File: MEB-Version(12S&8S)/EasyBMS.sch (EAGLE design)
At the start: 146 parts, among them IC1 XL7046, IC2 LTC6811IG-1#PBF, IC3 ESP32-S3-WROOM-1-N4R2, IC4 C98655, J1 TYPE-C-31-M-12, Q14 C8547, Q15 C8547, Q16 C8547, Q18 C8547, Q20 C8547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

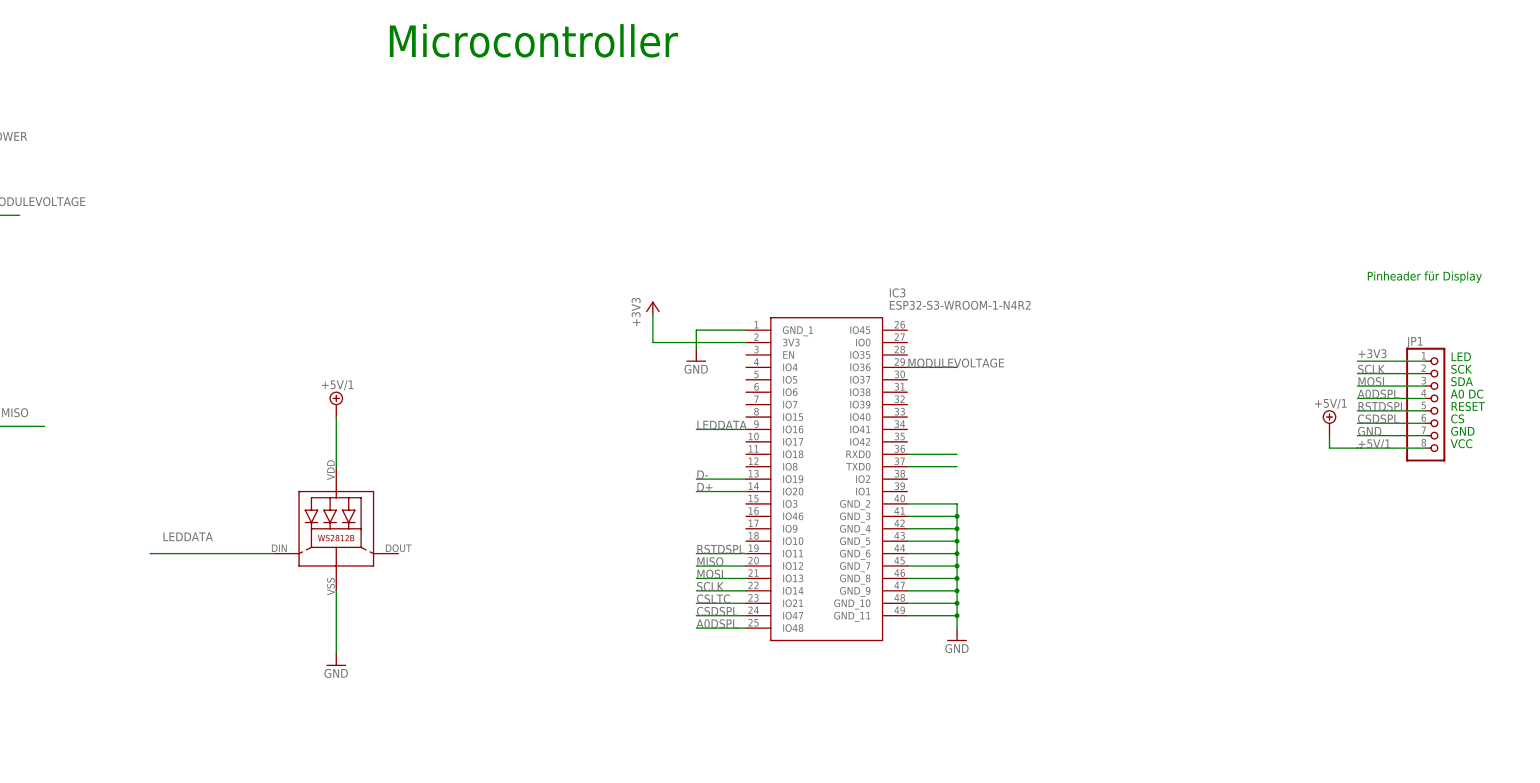
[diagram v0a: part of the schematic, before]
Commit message: add libraries folder with ESP32-C6 lib and change ESP32-S3 to ESP32-C6 MCU
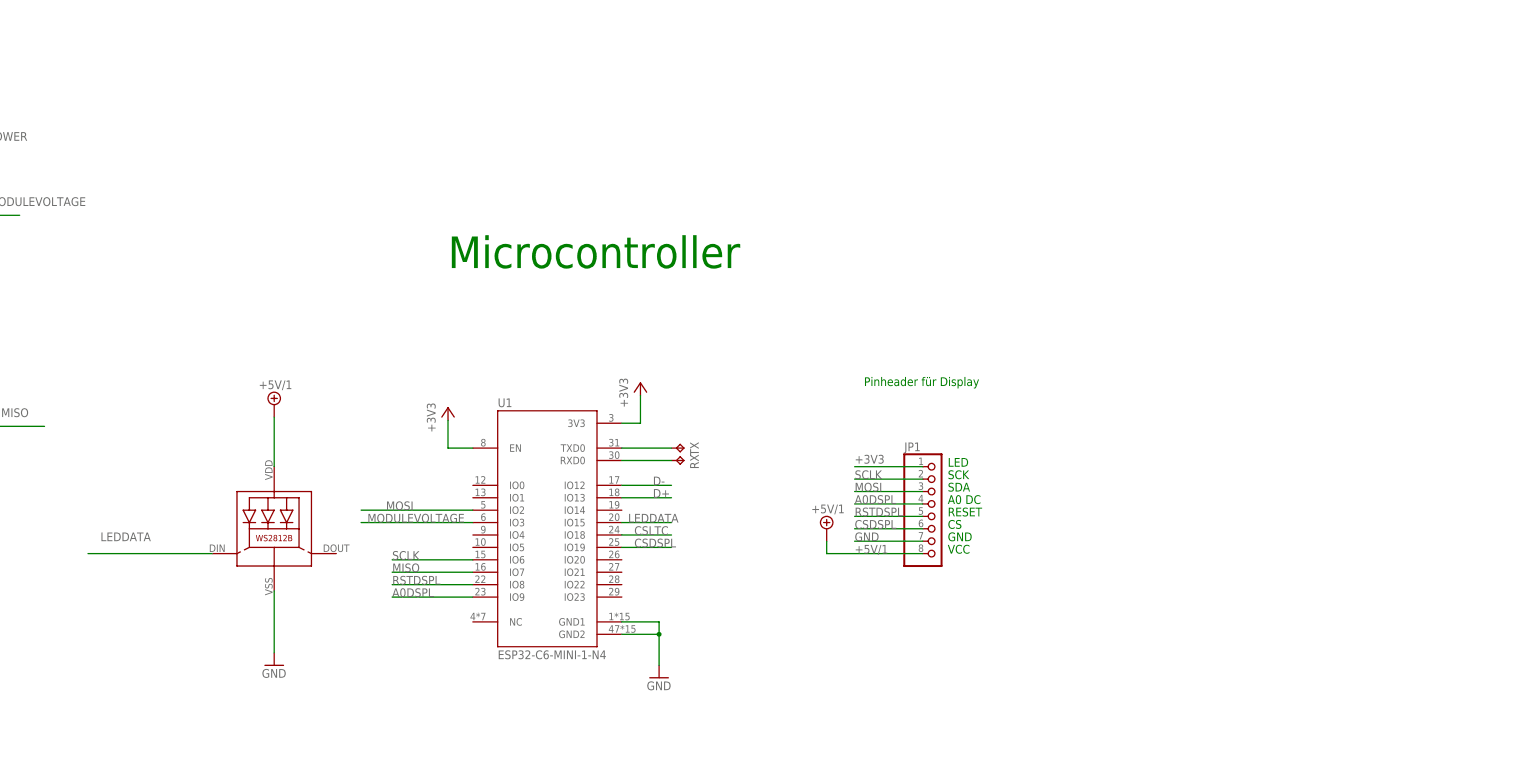
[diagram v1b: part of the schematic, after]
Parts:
- removed IC3: ESP32-S3-WROOM-1-N4R2, SamacSys_Parts:ESP32-S3-WROOM-1-N4R2
- added RX, TX: TPB2,54, testpad:TPB2,54
- added U1: ESP32-C6-MINI-1-N4, ESP32-C6-MINI-1-N4:ESP32-C6-MINI-1-N4
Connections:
- removed net N$51: IC3.RXD0
- removed net N$52: IC3.TXD0
- new net N$10: RX.TP, U1.RXD0
- new net N$2: TX.TP, U1.TXD0
- net +3V3: now also U1.3V3, U1.EN; no longer IC3.3V3
- net A0DSPL: now also U1.IO9; no longer IC3.IO48
- net CSDSPL: now also U1.IO19; no longer IC3.IO47
- net CSLTC: now also U1.IO18; no longer IC3.IO21
- net D+: now also U1.IO13; no longer IC3.IO20
- net D-: now also U1.IO12; no longer IC3.IO19
- net GND: now also U1.GND1, U1.GND2; no longer IC3.GND_1, IC3.GND_10, IC3.GND_11, IC3.GND_2, IC3.GND_3, IC3.GND_4, IC3.GND_5, IC3.GND_6, IC3.GND_7, IC3.GND_8, IC3.GND_9
- net LEDDATA: now also U1.IO15; no longer IC3.IO16
- net MISO: now also U1.IO7; no longer IC3.IO12
- net MODULEVOLTAGE: now also U1.IO3; no longer IC3.IO36
- net MOSI: now also U1.IO2; no longer IC3.IO13
- net RSTDSPL: now also U1.IO8; no longer IC3.IO11
- net SCLK: now also U1.IO6; no longer IC3.IO14
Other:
- moved on the sheet: JP1

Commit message: new version v3.0 review layout, change some parts and add isolated CAN-transceiver
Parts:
- added C10, C11: 100nF, rcl:C-EUC0402
- added C12: 47µF, rcl:C-EUC1206
- added C9: (no value), rcl:CPOL-EU153CLV-0605
- added CS1, CSLTC, MISO: (no value), jumper:SJ
- added IC3: ISO1042DWV, ISO1042DWV:ISO1042DWV
- added JP7: 2828XX-4282834-4, Connector:2828XX-4282834-4
- added R12: 120R, rcl:R-EU_R0402
- C1, C19, C4, C5, C7, C8: device rcl:C-EUC1206 -> rcl:C-EUC0402
- C20: value 100n -> 100nF; device rcl:C-EUC1206 -> rcl:C-EUC0805
- C21: device rcl:C-EUC1206 -> rcl:C-EUC0805
- C27: device rcl:C-EUC1206 -> rcl:C-EUC0603
- C3: value 100n -> 100nF; device rcl:C-EUC1206 -> rcl:C-EUC0402
- IC1: LCSC (none) -> C2843193
- J1: LCSC (none) -> C165948
- JP1: value (none) -> PINHD-1X8; device pinhead:PINHD-1X8 -> Connector:PINHD-1X8
- R2: device rcl:R-EU_R1206 -> rcl:R-EU_R0402
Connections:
- new net N$1: IC3.TXD, U1.IO22
- new net N$11: IC3.RXD, U1.IO23
- new net N$12: C11.1, C12.1, IC3.VCC2, JP7.1
- new net N$13: CS1.1, IC3.CANH, JP7.2
- new net N$14: IC3.CANL, JP7.3, R12.1
- new net N$16: C11.2, C12.2, IC3.GND2, JP7.4
- new net N$19: CS1.2, R12.2
- net +3V3: now also C10.1, C9.+, IC3.VCC1
- net A0DSPL: now also MISO.2
- net CSDSPL: now also CSLTC.2
- net CSLTC: now also CSLTC.1
- net GND: now also C10.2, C9.-, IC3.GND1
- net MISO: now also MISO.1
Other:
- moved on the sheet: C7, C8, H1, H2, H3, IC4, JP1, R15, R16, R2, RX, TX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

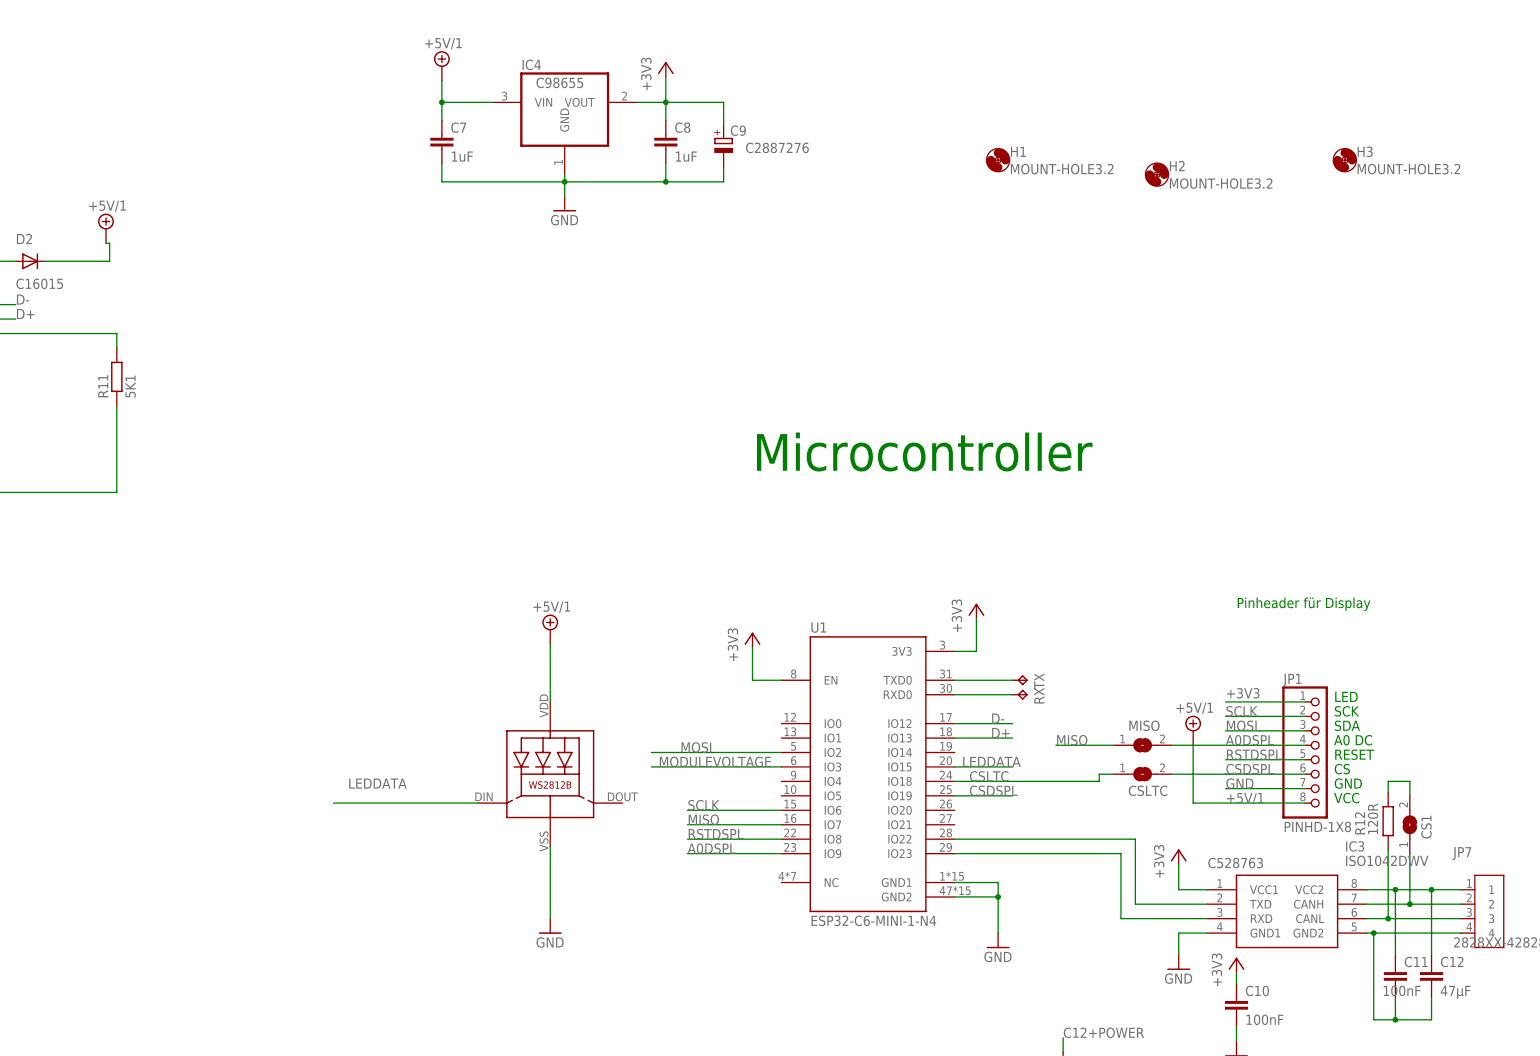
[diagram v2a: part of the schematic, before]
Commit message: add recommended aux parts for ESP module
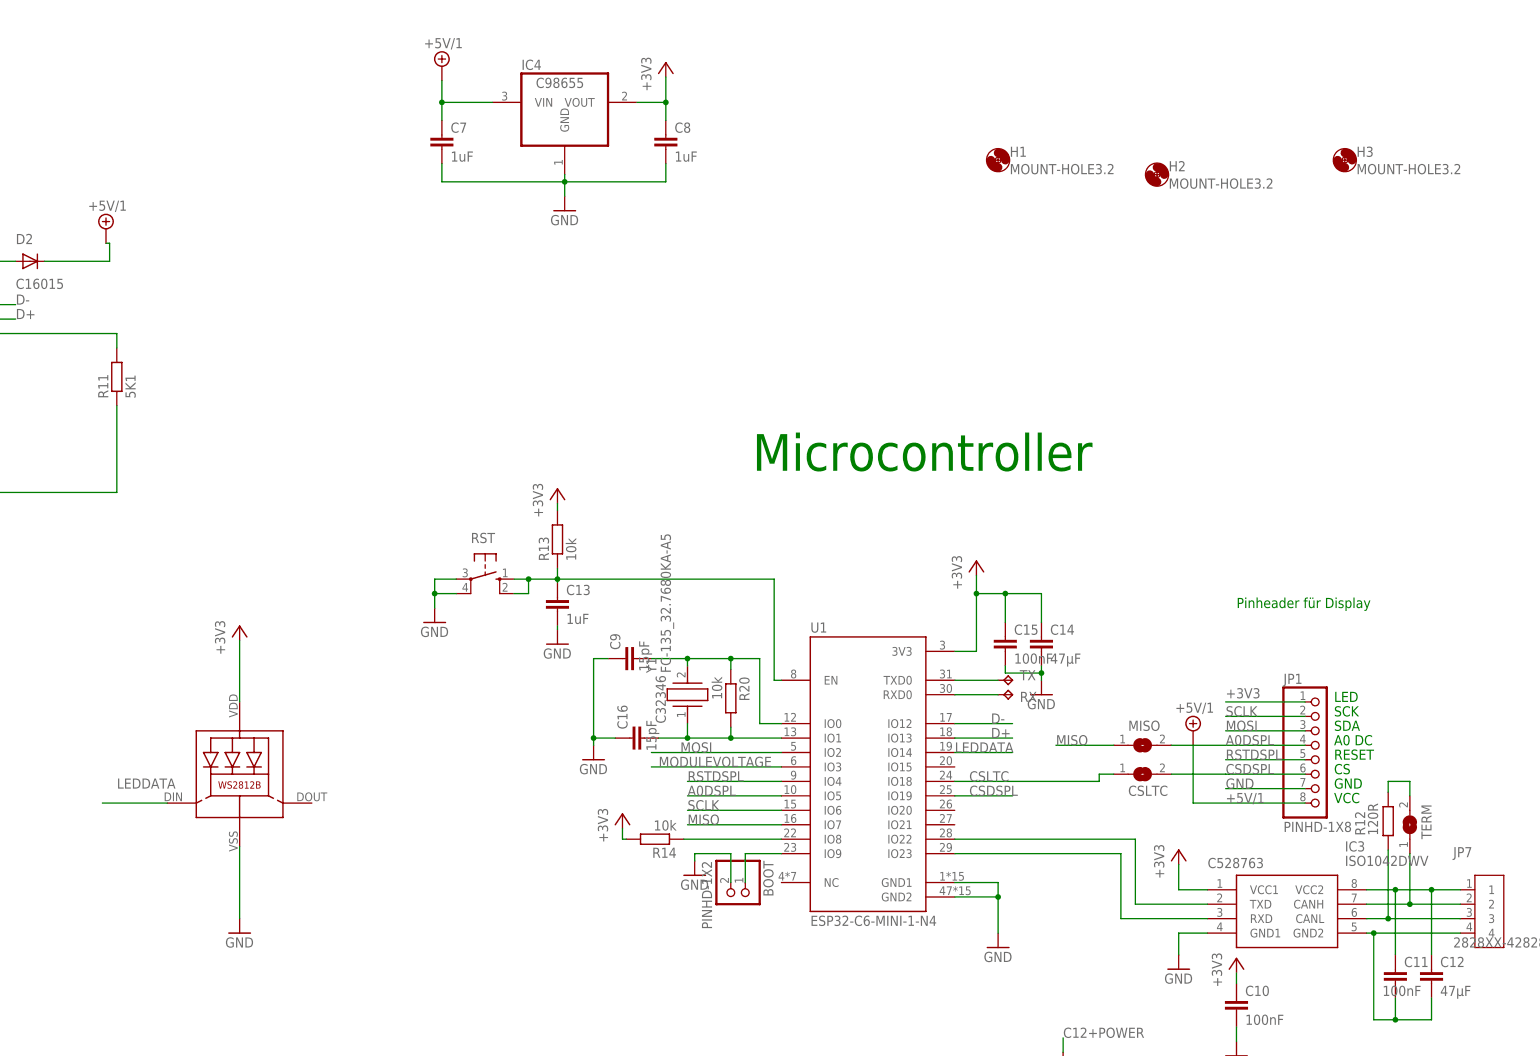
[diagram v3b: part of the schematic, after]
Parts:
- added BOOT: PINHD-1X2, Connector:PINHD-1X2
- added C13: 1uF, rcl:C-EUC0402
- added C14: 47µF, rcl:C-EUC1206
- added C15: 100nF, rcl:C-EUC0402
- added C16: 15pF, rcl:C-EUC0402
- added R13, R14, R20: 10k, rcl:R-EU_R0402
- added RST: (no value), switch-omron:10-XX
- added Y1: FC-135_32.7680KA-A5, FC-135_32.7680KA-A5:FC-135_32.7680KA-A5
- C9: value (none) -> 15pF; device rcl:CPOL-EU153CLV-0605 -> rcl:C-EUC0402; LCSC C2887276 -> (none)
- renumbered CS1 to TERM
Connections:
- new net N$17: C13.1, R13.1, RST.S, RST.S1, U1.EN
- new net N$20: R14.1, U1.IO8
- new net N$21: BOOT.1, U1.IO9
- new net N$22: C9.2, R20.1, U1.IO0, Y1.2
- new net N$23: C16.2, R20.2, U1.IO1, Y1.1
- net +3V3: now also C14.1, C15.1, LED2.VDD, R13.2, R14.2; no longer C9.+, U1.EN
- net +5V/1: no longer LED2.VDD
- net A0DSPL: now also U1.IO5; no longer U1.IO9
- net GND: now also BOOT.2, C13.2, C14.2, C15.2, C16.1, C9.1, RST.P, RST.P1; no longer C9.-
- net LEDDATA: now also U1.IO14; no longer U1.IO15
- net RSTDSPL: now also U1.IO4; no longer U1.IO8
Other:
- moved on the sheet: RX, TX
